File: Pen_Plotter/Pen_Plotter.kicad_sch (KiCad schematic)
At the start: 38 parts, among them J1 USB_Type-C_Breakout, J2 PinHeader_01x05_P2.54mm_Verti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, J3 PinHeader_01x05_P2.54mm_Verti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, J4 Screw_Terminal_01x02_P3.5mm, J5 PinHeader_01x02_P2.54mm_Verti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, J6 PinHeader_01x02_P2.54mm_Verti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, J7 PinHeader_01x03_P2.54mm_Verti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, Q1 Transistor_MOSFET_NCh_SOT23, Q2 Transistor_MOSFET_NCh_SOT23, SW1 Switch_Tactile_Omron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

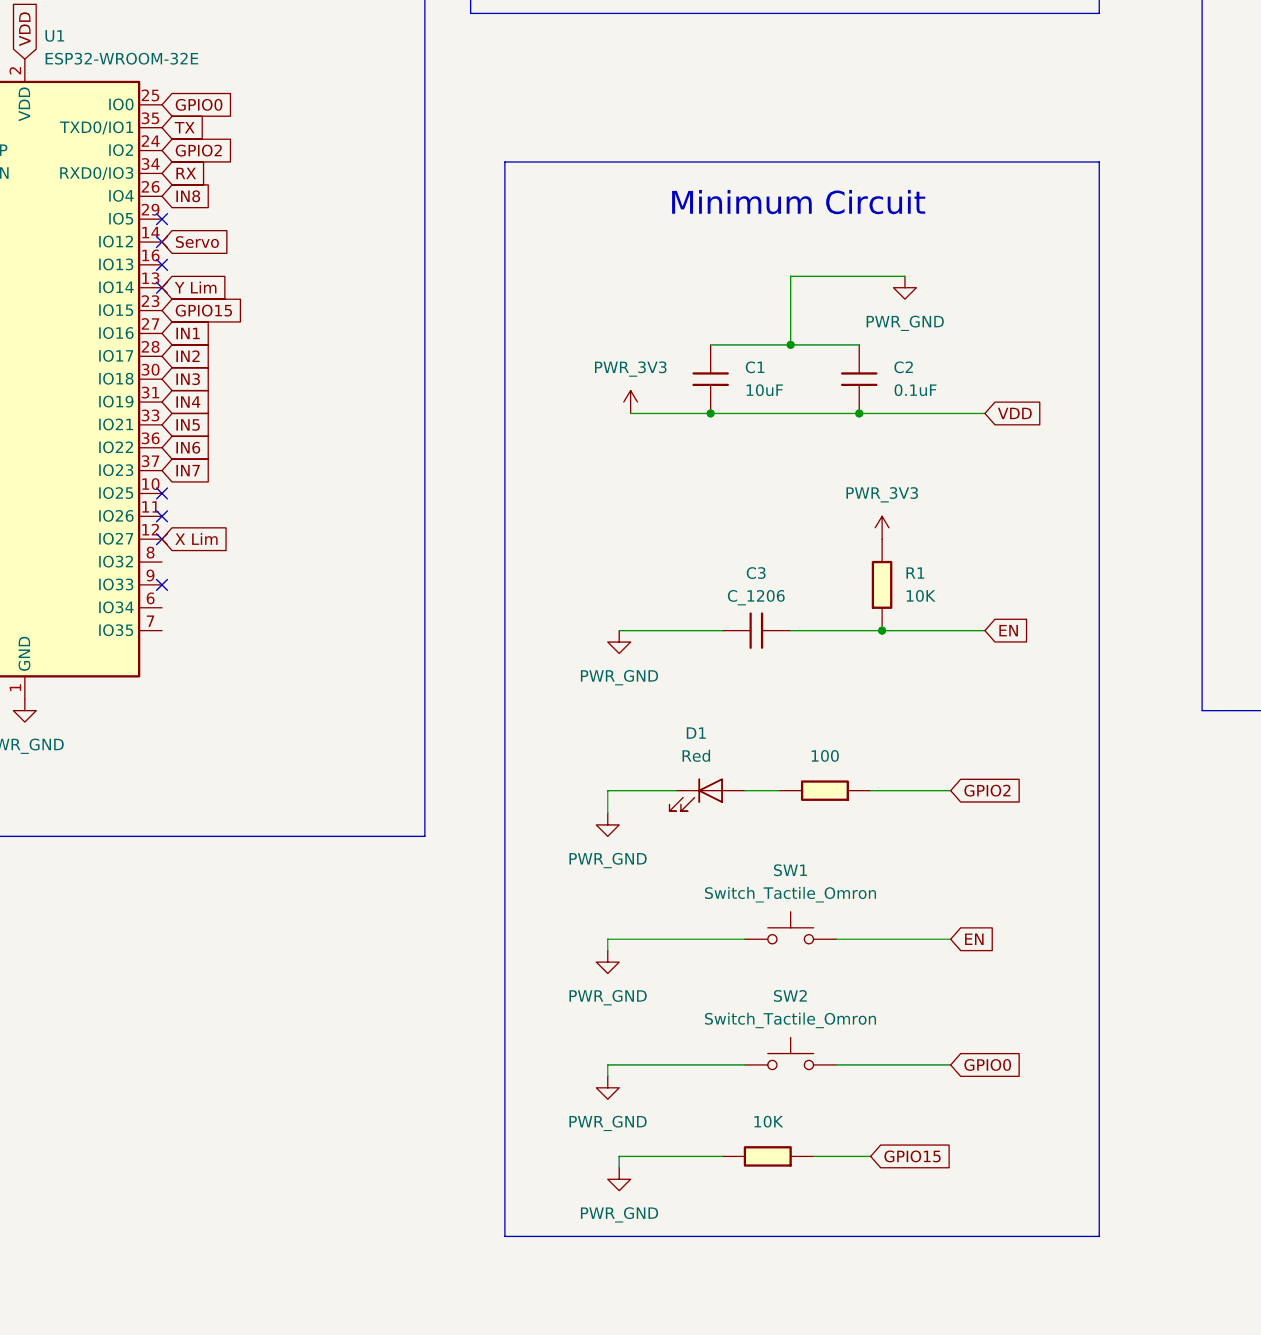
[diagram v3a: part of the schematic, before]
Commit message: Version with Auto Programmer, USBC and CH340 IC
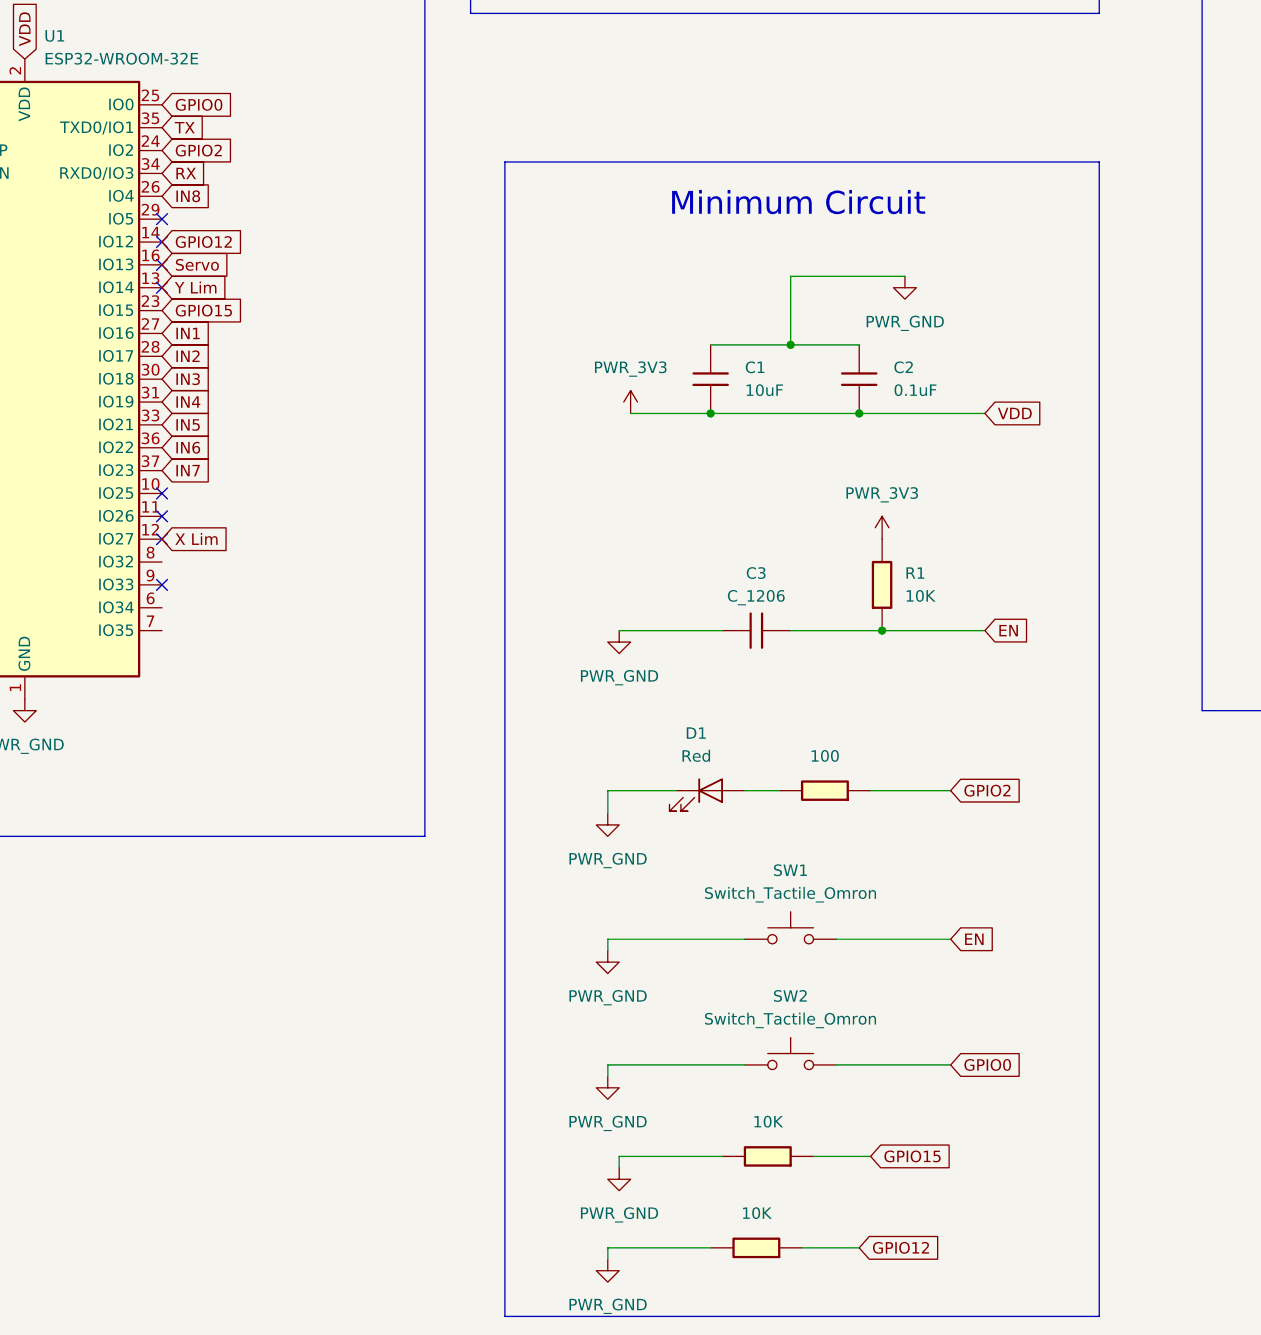
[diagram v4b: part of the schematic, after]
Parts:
- added R11: 10K, fab:R_1206, symbol fab:R_1206
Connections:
- net PWR_GND: now also R11.1
- net Servo: now also U1.16 (IO13); no longer U1.14 (IO12)
- new net GPIO12: R11.2, U1.14 (IO12)
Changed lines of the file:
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@@
 	(rectangle
 		(start 233.68 83.82)
-		(end 299.72 203.2)
+		(end 299.72 212.09)
 		(stroke
 			(width 0)
@@
 	(wire
 		(pts
+			(xy 266.7 204.47) (xy 273.05 204.47)
+		)
+		(stroke
+			(width 0)
+			(type default)
+		)
+	)
+	(wire
+		(pts
 			(xy 337.82 48.26) (xy 337.82 50.8)
 		)
@@
 	(wire
 		(pts
+			(xy 245.11 205.74) (xy 245.11 204.47)
+		)
+		(stroke
+			(width 0)
+			(type default)
+		)
+	)
+	(wire
+		(pts
 			(xy 361.95 124.46) (xy 359.41 124.46)
 		)
@@
 	(wire
 		(pts
+			(xy 245.11 204.47) (xy 256.54 204.47)
+		)
+		(stroke
+			(width 0)
+			(type default)
+		)
+	)
+	(wire
+		(pts
 			(xy 96.52 140.97) (xy 97.79 140.97)
 		)
@@
 		)
 	)
+	(global_label "GPIO12"
+		(shape input)
+		(at 273.05 204.47 0)
+		(fields_autoplaced yes)
+		(effects
+			(font
+				(size 1.27 1.27)
+			)
+			(justify left)
+		)
+		(property "Intersheetrefs" "${INTERSHEET_REFS}"
+			(at 282.9295 204.47 0)
+			(effects
+				(font
+					(size 1.27 1.27)
+				)
+				(justify left)
+				(hide yes)
+			)
+		)
+	)
 	(global_label "IN1"
 		(shape input)
@@
 		)
 	)
+	(global_label "GPIO12"
+		(shape input)
+		(at 195.58 92.71 0)
+		(fields_autoplaced yes)
+		(effects
+			(font
+				(size 1.27 1.27)
+			)
+			(justify left)
+		)
+		(property "Intersheetrefs" "${INTERSHEET_REFS}"
+			(at 205.4595 92.71 0)
+			(effects
+				(font
+					(size 1.27 1.27)
+				)
+				(justify left)
+				(hide yes)
+			)
+		)
+	)
 	(global_label "IN7"
 		(shape input)
@@
 	(global_label "Servo"
 		(shape input)
-		(at 195.58 92.71 0)
+		(at 195.58 95.25 0)
 		(fields_autoplaced yes)
 		(effects
@@
 		)
 		(property "Intersheetrefs" "${INTERSHEET_REFS}"
-			(at 203.7661 92.71 0)
+			(at 203.7661 95.25 0)
 			(effects
 				(font
@@
 	)
 	(symbol
+		(lib_id "fab:PWR_GND")
+		(at 245.11 205.74 0)
+		(unit 1)
+		(exclude_from_sim no)
+		(in_bom yes)
+		(on_board yes)
+		(dnp no)
+		(fields_autoplaced yes)
+		(property "Reference" "#PWR034"
+			(at 245.11 212.09 0)
+			(effects
+				(font
+					(size 1.27 1.27)
+				)
+				(hide yes)
+			)
+		)
+		(property "Value" "PWR_GND"
+			(at 245.11 210.82 0)
+			(effects
+				(font
+					(size 1.27 1.27)
+				)
+			)
+		)
+		(property "Footprint" ""
+			(at 245.11 205.74 0)
+			(effects
+				(font
+					(size 1.27 1.27)
+				)
+				(hide yes)
+			)
+		)
+		(property "Datasheet" ""
+			(at 245.11 205.74 0)
+			(effects
+				(font
+					(size 1.27 1.27)
+				)
+				(hide yes)
+			)
+		)
+		(property "Description" "Power symbol creates a global label with name \"GND\" , ground"
+			(at 245.11 205.74 0)
+			(effects
+				(font
+					(size 1.27 1.27)
+				)
+				(hide yes)
+			)
+		)
+		(pin "1"
+		)
+		(instances
+			(project "Pen_Plotter"
+				(path "/4e9b223a-cbc5-44ea-8094-5eb0dbc835d2"
+					(reference "#PWR034")
+					(unit 1)
+				)
+			)
+		)
+	)
+	(symbol
 		(lib_id "fab:Switch_Tactile_Omron")
 		(at 265.43 170.18 0)
@@
 					(unit 1)
 				)
+			)
+		)
+	)
+	(symbol
+		(lib_id "fab:R_1206")
+		(at 261.62 204.47 90)
+		(unit 1)
+		(exclude_from_sim no)
+		(in_bom yes)
+		(on_board yes)
+		(dnp no)
+		(fields_autoplaced yes)
+		(property "Reference" "R11"
+			(at 261.62 198.12 90)
+			(effects
+				(font
+					(size 1.27 1.27)
+				)
+				(hide yes)
+			)
+		)
+		(property "Value" "10K"
+			(at 261.62 200.66 90)
+			(effects
+				(font
+					(size 1.27 1.27)
+				)
+			)
+		)
+		(property "Footprint" "fab:R_1206"
+			(at 261.62 204.47 90)
+			(effects
+				(font
+					(size 1.27 1.27)
+				)
+				(hide yes)
+			)
+		)
+		(property "Datasheet" "~"
+			(at 261.62 204.47 0)
+			(effects
+				(font
+					(size 1.27 1.27)
+				)
+				(hide yes)
+			)
+		)
+		(property "Description" "Resistor"
+			(at 261.62 204.47 0)
+			(effects
+				(font
+					(size 1.27 1.27)
+				)
+				(hide yes)
+			)
+		)
+		(pin "1"
+		)
+		(pin "2"
+		)
+		(instances
+			(project "Pen_Plotter"
+				(path "/4e9b223a-cbc5-44ea-8094-5eb0dbc835d2"
+					(reference "R11")
+					(unit 1)
+				)

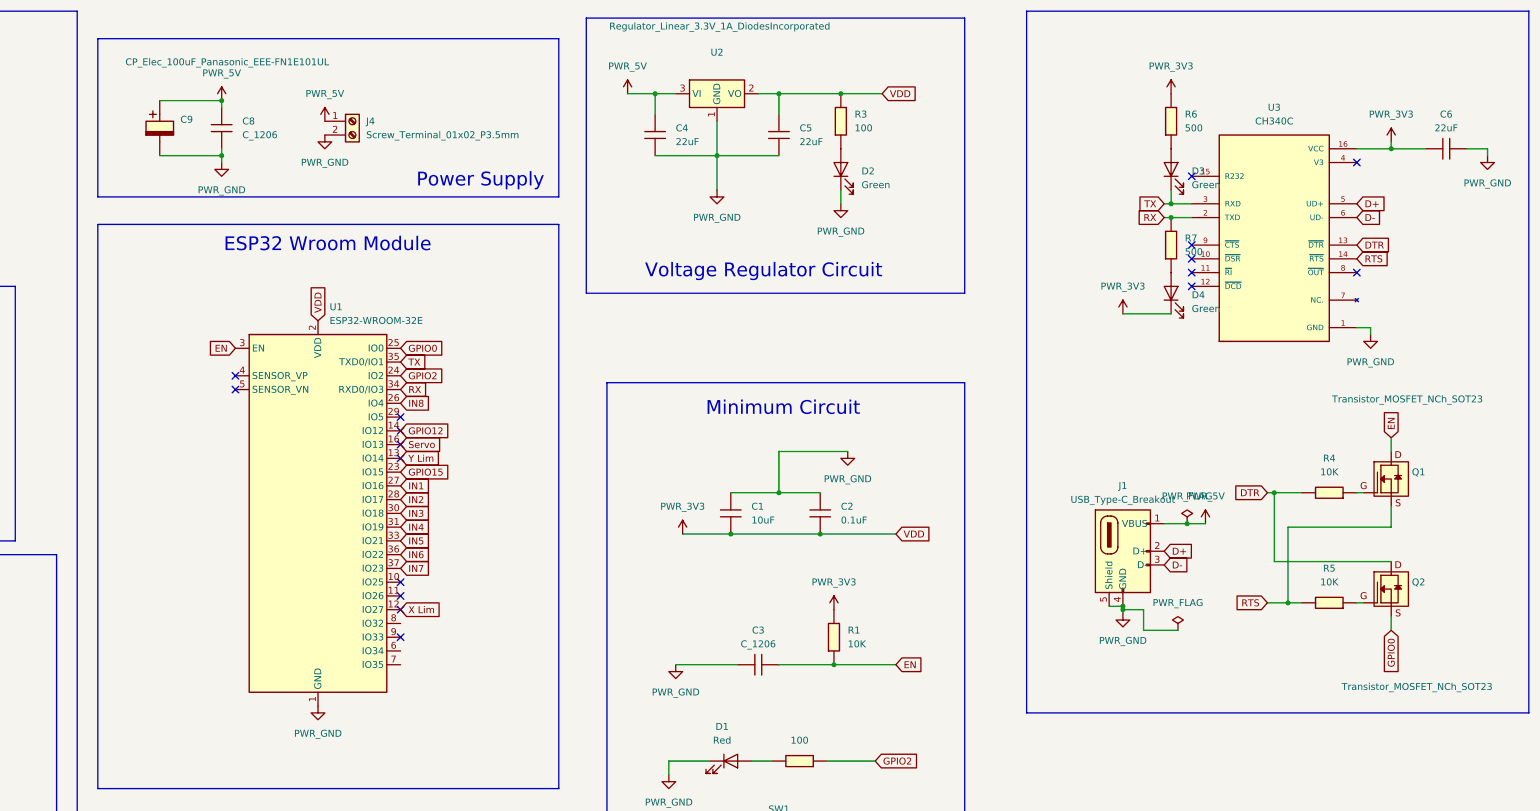
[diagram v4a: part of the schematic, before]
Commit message: Schematic Excluded USBC, CH340IC, Autoprogrammer PCB: Removed components
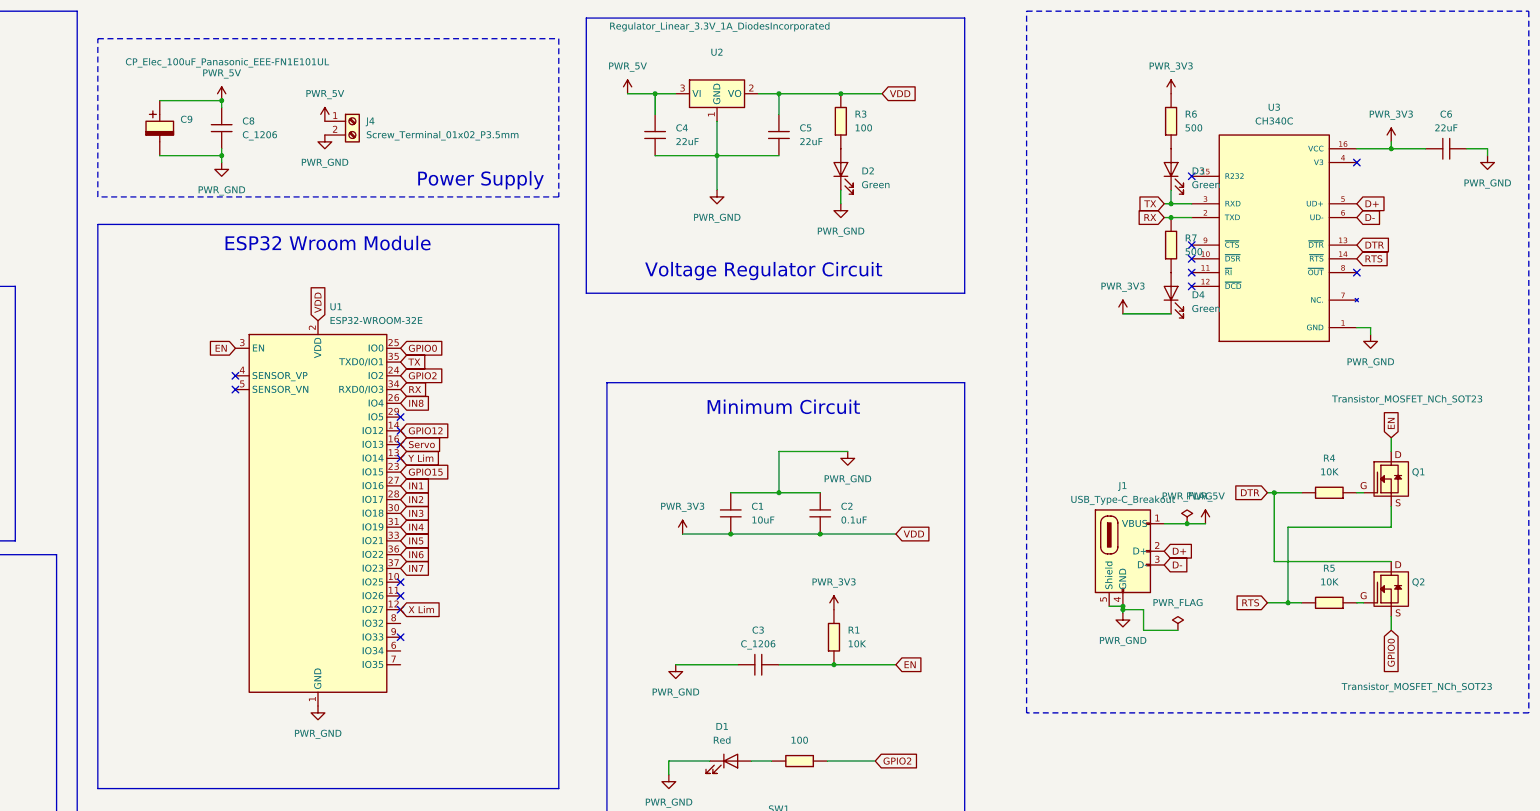
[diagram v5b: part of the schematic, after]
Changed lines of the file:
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@@
 		(end 224.79 49.53)
 		(stroke
-			(width 0)
-			(type default)
+			(width 0.127)
+			(type dash)
+			(color 255 7 0 1)
 		)
 		(fill
@@
 		(end 403.86 144.78)
 		(stroke
-			(width 0)
-			(type default)
+			(width 0.127)
+			(type dash)
+			(color 255 0 0 1)
 		)
 		(fill
@@
 		(exclude_from_sim no)
 		(in_bom yes)
-		(on_board yes)
+		(on_board no)
 		(dnp no)
 		(fields_autoplaced yes)
@@
 		(exclude_from_sim no)
 		(in_bom yes)
-		(on_board yes)
+		(on_board no)
 		(dnp no)
 		(fields_autoplaced yes)
@@
 		(exclude_from_sim no)
 		(in_bom yes)
-		(on_board yes)
+		(on_board no)
 		(dnp no)
 		(fields_autoplaced yes)

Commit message: PCB for ESP UCap
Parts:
- removed C6: 22uF, fab:C_1206, symbol fab:C_1206
- removed D3, D4: Green, fab:LED_1206, symbol fab:LED_1206
- removed J1: USB_Type-C_Breakout, Proshplay Type C:ProshPlay-Type-C-breakout-board, symbol ProshPlay:ProshPlay-Type-C-breakout-board
- removed J4: Screw_Terminal_01x02_P3.5mm, fab:TerminalBlock_OnShore_1x02_P3.50mm_Horizontal, symbol fab:Screw_Terminal_01x02_P3.5mm
- removed Q1, Q2: Transistor_MOSFET_NCh_SOT23, fab:SOT-23-3, symbol fab:Transistor_MOSFET_NCh_SOT23
- removed R7: 500, fab:R_1206, symbol fab:R_1206
- removed U3: CH340C, CH340C:SOIC127P600X180-16N, symbol CH340C:CH340C
- added J4: Conn_02x03_Counter_Clockwise, Connector_PinHeader_2.54mm:PinHeader_2x03_P2.54mm_Horizontal, symbol Connector_Generic:Conn_02x03_Counter_Clockwise
- R6: value 500 -> 0
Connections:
- net DTR is gone; now on net PWR_3V3: R4.1
- net RTS is gone; now on net PWR_3V3: R5.1
- net EN: now also R5.2, J4.2 (Pin_2)
- net GPIO0: now also R4.2, J4.3 (Pin_3)
- net IN1: now also U1.37 (IO23); no longer U1.27 (IO16)
- net IN2: now also U1.36 (IO22); no longer U1.28 (IO17)
- net IN3: now also U1.33 (IO21); no longer U1.30 (IO18)
- net IN5: now also U1.30 (IO18); no longer U1.33 (IO21)
- net IN6: now also U1.28 (IO17); no longer U1.36 (IO22)
- net IN7: now also U1.27 (IO16); no longer U1.37 (IO23)
- net PWR_3V3: no longer R6.1
- net PWR_5V: now also J4.1 (Pin_1)
- net PWR_GND: now also J4.5 (Pin_5)
- net RX: now also J4.6 (Pin_6)
- net TX: now also R6.1, R6.2, J4.4 (Pin_4)
- no-connect marks 17 -> 10
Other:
- note added: "ESP32 Auto Programmer - Type C"

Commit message: Mini Plotter PCB 13
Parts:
- added J1: USB4125-GF-A_REVA2, USB4125-GF-A_REVA2:GCT_USB4125-GF-A_REVA2, symbol USB4125-GF-A_REVA2:USB4125-GF-A_REVA2
- added R7: 0, fab:R_1206, symbol fab:R_1206
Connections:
- net EN: now also R7.1, R7.2
- net PWR_5V: now also J1.A9 (VBUS), J1.B9 (VBUS__1)
- net PWR_GND: now also J1.A12 (GND), J1.B12 (GND__1), J1.S1 (SHIELD), J1.S2 (SHIELD__1), J1.S3 (SHIELD__2), J1.S4 (SHIELD__3)
- no-connect marks 10 -> 12
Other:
- moved on the sheet: C8, C9

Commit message: Added gerber files
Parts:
- added H1, H2, H3, H4: ~, fab:MountingHole_M3, symbol fab:MountingHole_M3
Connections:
- no-connect marks 12 -> 13
